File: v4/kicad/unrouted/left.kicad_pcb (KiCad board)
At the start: 2 copper layers, 158 x 119 mm, 68 parts

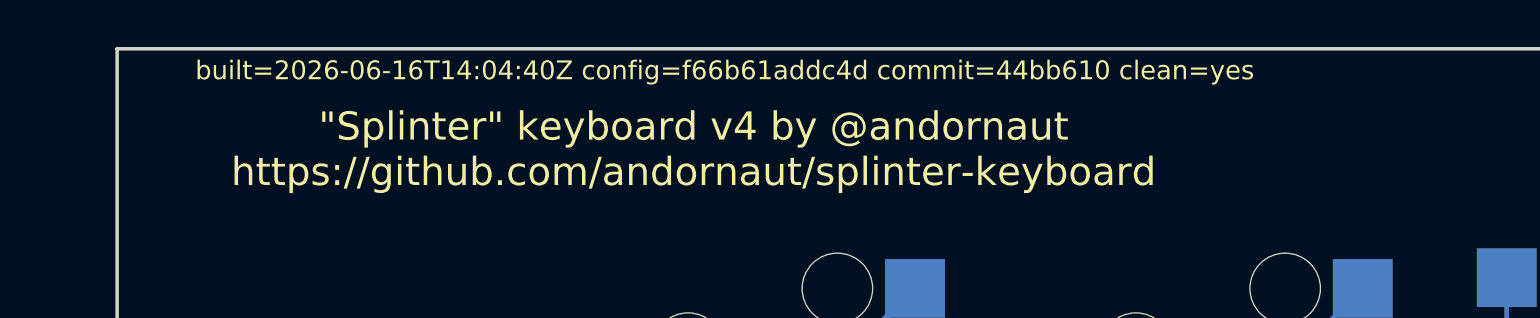
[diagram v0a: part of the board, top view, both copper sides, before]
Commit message: v4: restore right-half teardrops on routed + unrouted masters
The right master carried only 20 teardrop zones (the teardrop-loss
failure that shipped on the first JLCPCB order); re-teardropped to 502,
now symmetric with the left half (464). Tracks, vias, and arcs are
unchanged on both halves (408/70/128 right, 384/65/120 left); the rest
of the diff is KiCad re-save churn. Clears the validate:fab
teardrop-consistency gate.
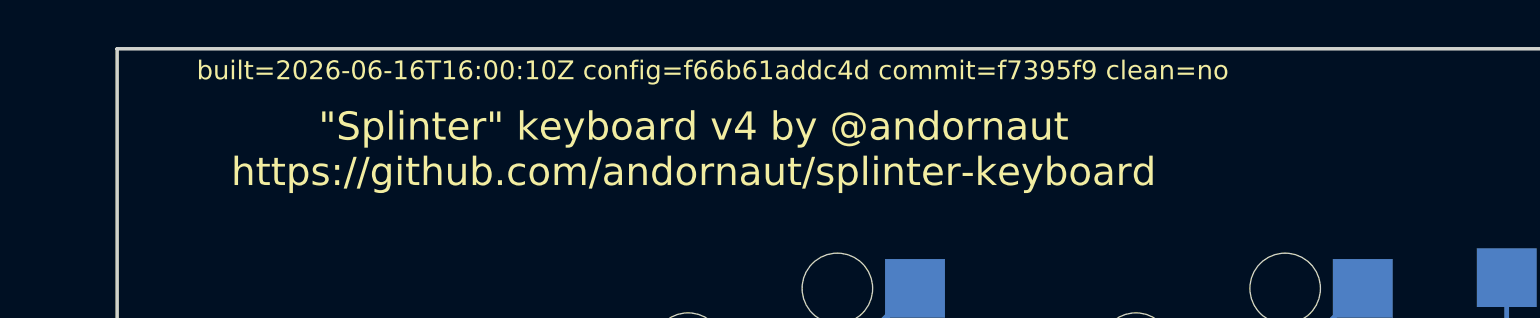
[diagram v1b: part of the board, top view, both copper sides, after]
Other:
- board text added: "built=2026-06-16T16:00:10Z config=f66b61addc4d commit=f7395f9 clean=no"
- board text removed: "built=2026-06-16T14:04:40Z config=f66b61addc4d commit=44bb610 clean=yes"

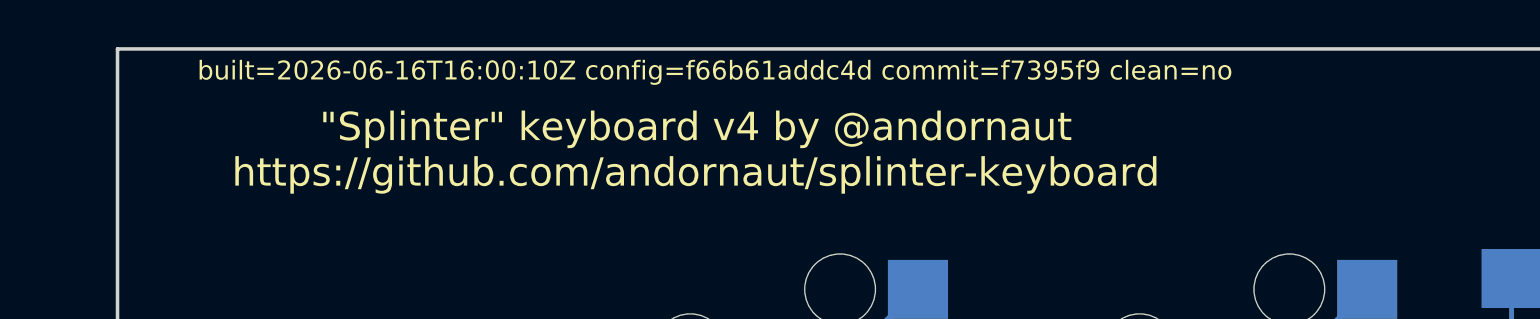
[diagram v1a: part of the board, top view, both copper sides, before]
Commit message: v4: fabrication build (ordering this from JLCPCB)
Validated fab-ready and sent to JLCPCB. Teardrops symmetric (459 left /
496 right zones), GND pour filled on B.Cu (~13000mm^2 master, ~157x118mm
flood in the shipped B_Cu gerber), DRC clean (0 violations / 0 unconnected
both halves), provenance matches config, gerber set + assembly complete.

Provenance stamp (routed masters):
  splinter v=v4 built=2026-06-16T16:30:02Z config=f66b61addc4d commit=d2fd01a clean=yes
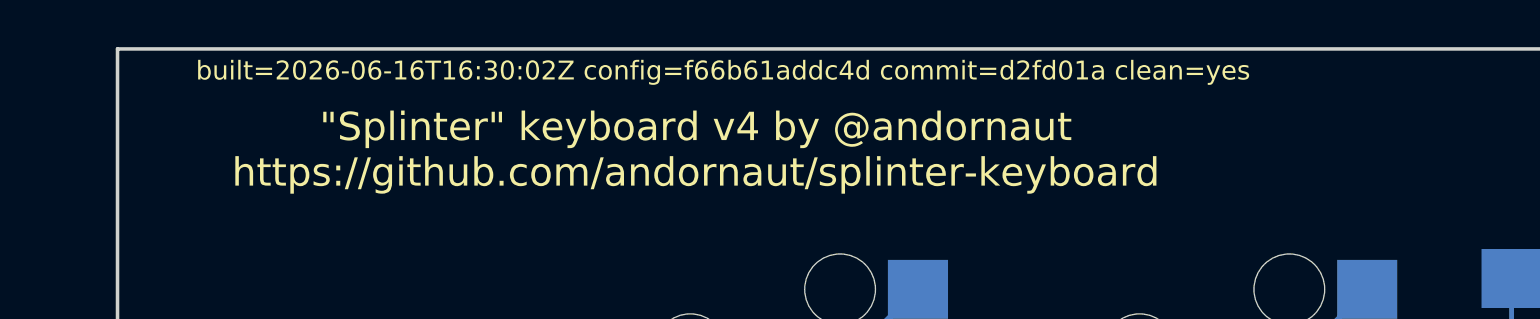
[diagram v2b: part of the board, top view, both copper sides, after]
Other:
- board text added: "built=2026-06-16T16:30:02Z config=f66b61addc4d commit=d2fd01a clean=yes"
- board text removed: "built=2026-06-16T16:00:10Z config=f66b61addc4d commit=f7395f9 clean=no"

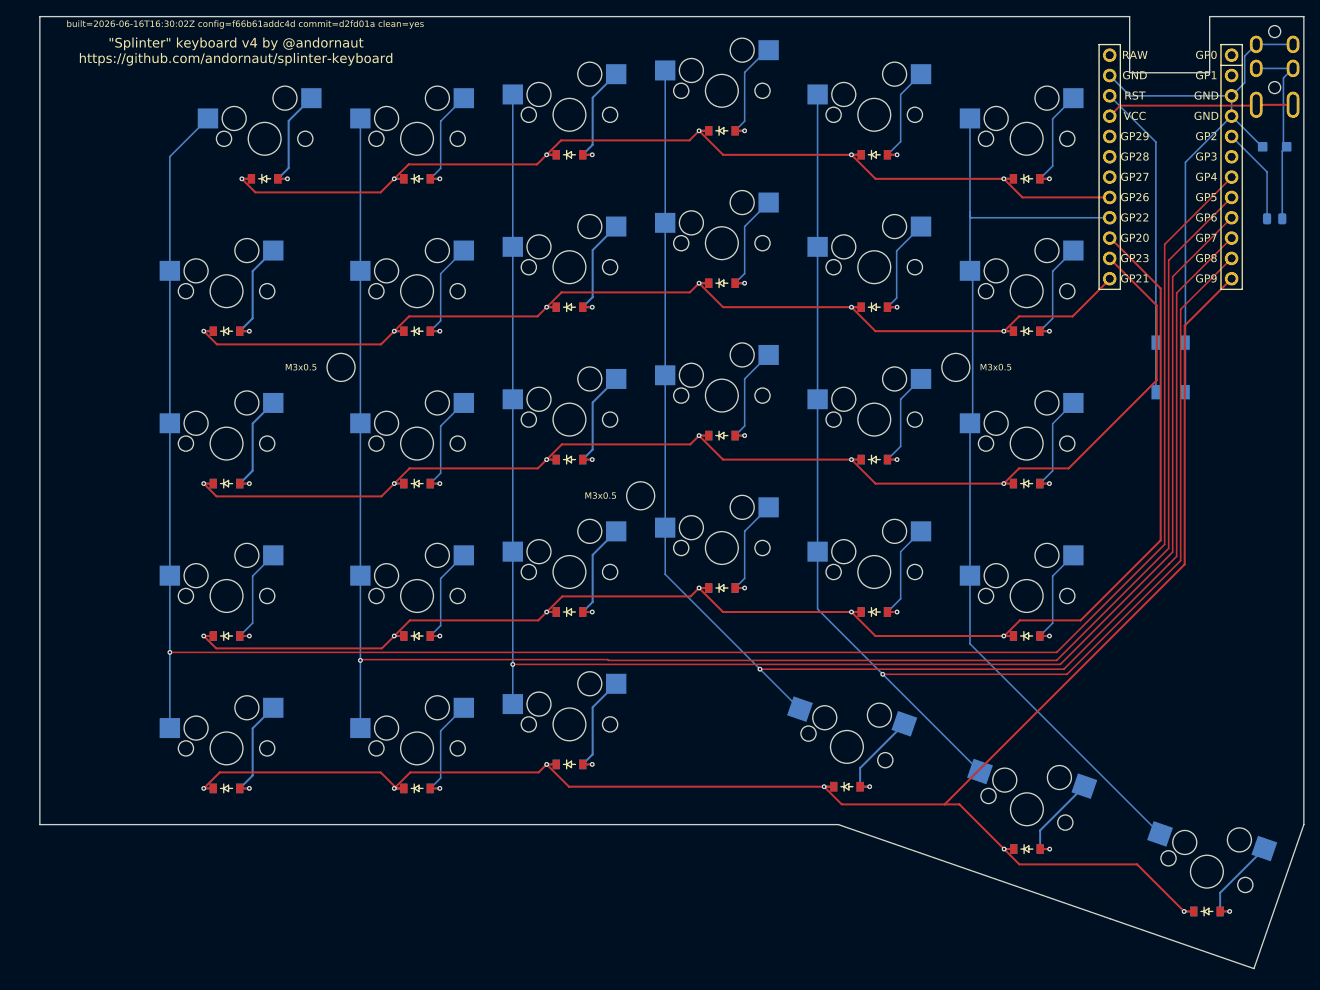
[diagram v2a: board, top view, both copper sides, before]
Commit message: v4: square-cornered USB-C notch, unified 0.25mm clearance, onshape case notes
- config: subtract the USB-C cutout (_usbleft/_usbright) after the exterior
  fillet so the notch keeps square corners; tie it to mcu_reset_x so it tracks
  the MCU. Nudge MCU/reset/TRRS/TVS/resistor placement.
- apply-project-settings: add ensure_default_clearance so the Default net class
  clearance is 0.25mm, unifying the gap with VCC across the board.
- regenerate routed + unrouted boards and project files.
- onshape: add v4 case design guidance (FDM + JLCCNC sandwich topology).
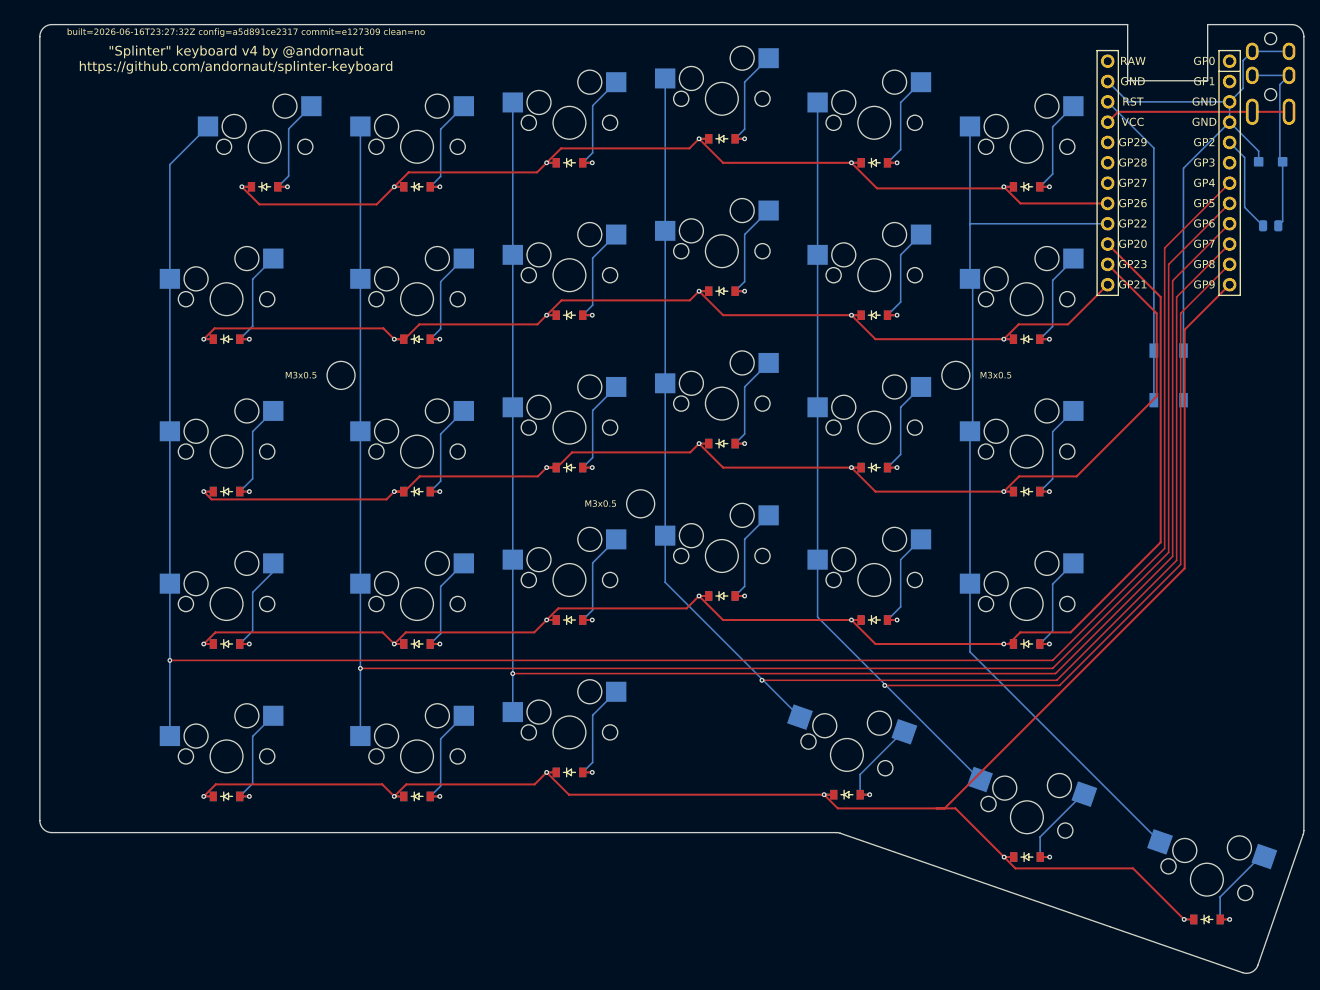
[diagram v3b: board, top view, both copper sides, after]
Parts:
- moved D31 1.94 mm to (284.8, 106.7)
- moved B1 1.03 mm to (272.0, 133.4)
- moved R1 1.01 mm to (284.8, 114.7)
- moved TRRS1 1.01 mm to (284.8, 89.7)
- moved D1 1.00 mm to (154.2, 186.0)
- moved D10 1.00 mm to (178.1, 109.8)
- moved D11 1.00 mm to (197.1, 183.0)
- moved D12 1.00 mm to (197.1, 163.9)
- moved D13 1.00 mm to (197.1, 144.9)
- moved D14 1.00 mm to (197.1, 125.8)
- moved D15 1.00 mm to (197.1, 106.8)
- moved D16 1.00 mm to (216.2, 160.9)
- moved D17 1.00 mm to (216.2, 141.9)
- moved D18 1.00 mm to (216.2, 122.8)
- moved D19 1.00 mm to (216.2, 103.8)
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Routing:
- net P9: track 229.5 -> 228.3 mm
- net GND: track 73.4 -> 74.5 mm
- net zero_lower: track 14.2 -> 13.2 mm
- net P15: track 116.6 -> 115.8 mm
- net P14: track 185.6 -> 184.9 mm
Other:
- board size 158 x 119 mm -> 158 x 118.6 mm
- board text added: "built=2026-06-16T23:27:32Z config=a5d891ce2317 commit=e127309 clean=no"
- board text removed: "built=2026-06-16T16:30:02Z config=f66b61addc4d commit=d2fd01a clean=yes"

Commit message: v4: rebuild boards, restamp provenance clean=yes at fbbf6c4
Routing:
- net P14: track 184.9 -> 186.1 mm
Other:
- board text added: "built=2026-06-17T00:36:15Z config=a5d891ce2317 commit=fbbf6c4 clean=yes"
- board text removed: "built=2026-06-16T23:27:32Z config=a5d891ce2317 commit=e127309 clean=no"

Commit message: checkpoint
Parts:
- removed MH3: , ceoloide:mounting_hole_npth
- moved MH2 42.7 mm to (245.5, 133.4)
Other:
- board text added: "built=2026-06-21T00:07:01Z config=219748922ef7 commit=e35136f clean=no"
- board text removed: "built=2026-06-17T00:36:15Z config=a5d891ce2317 commit=fbbf6c4 clean=yes"

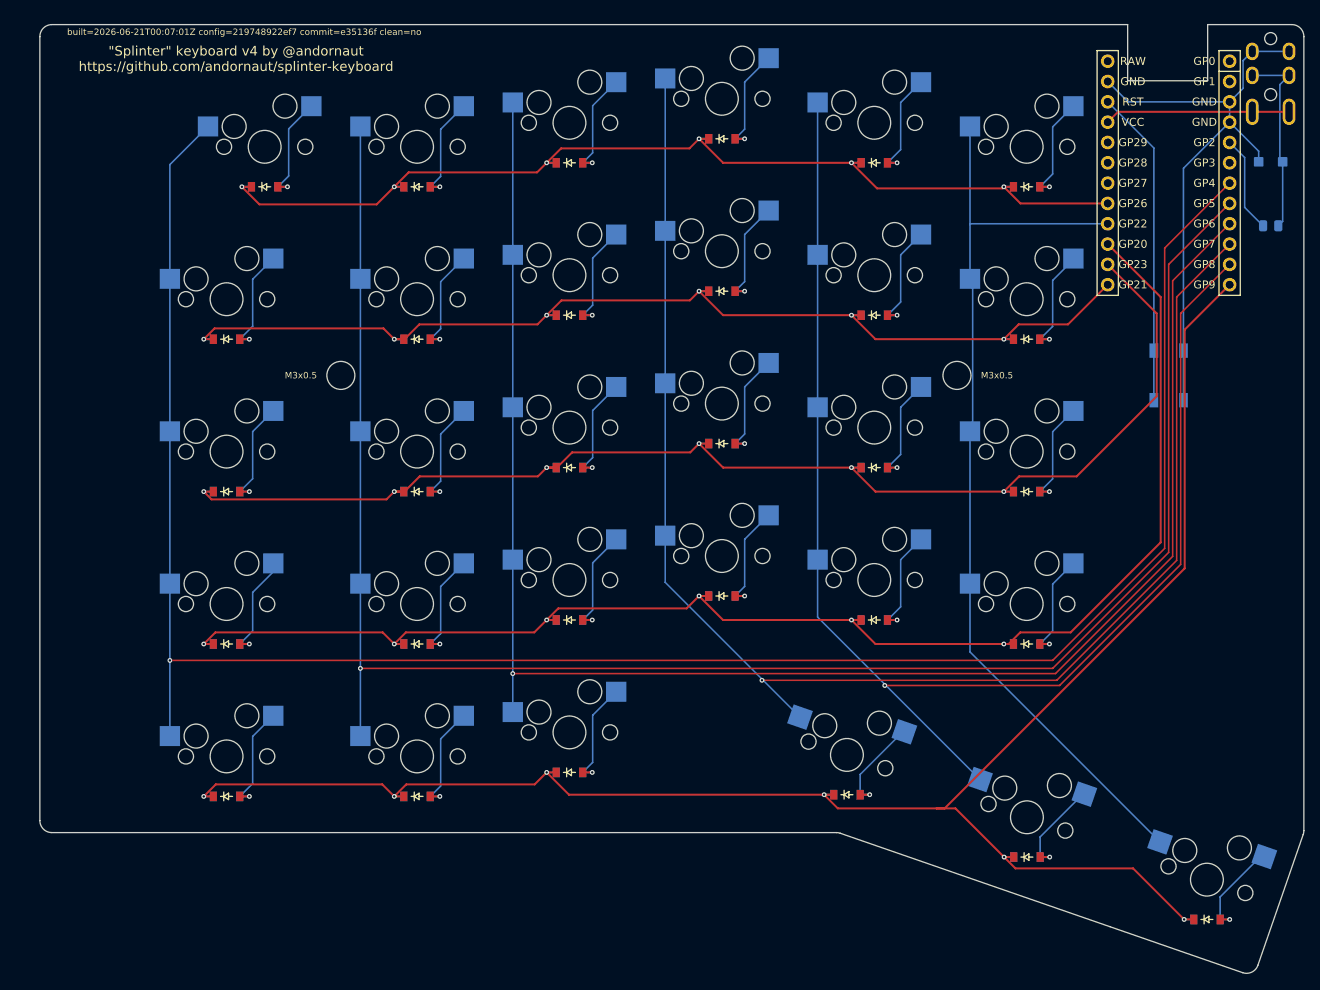
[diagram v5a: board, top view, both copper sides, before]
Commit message: v4: single center support post, retune screws, named boss/support radii
- Replace the three anti-flex support posts with one center-top post
- Reposition screw holes into the diagonal key gaps so the boss clears
  the 14.5mm switch cutouts on both halves
- Promote the boss/support radii to named units (boss 2.5 -> 2.75mm,
  support 2.5 -> 2.25mm) instead of hardcoded literals
- Factor shared silk text geometry into a &text_style YAML anchor
- Trim stale/redundant config comments
- Regenerate unrouted PCBs to match
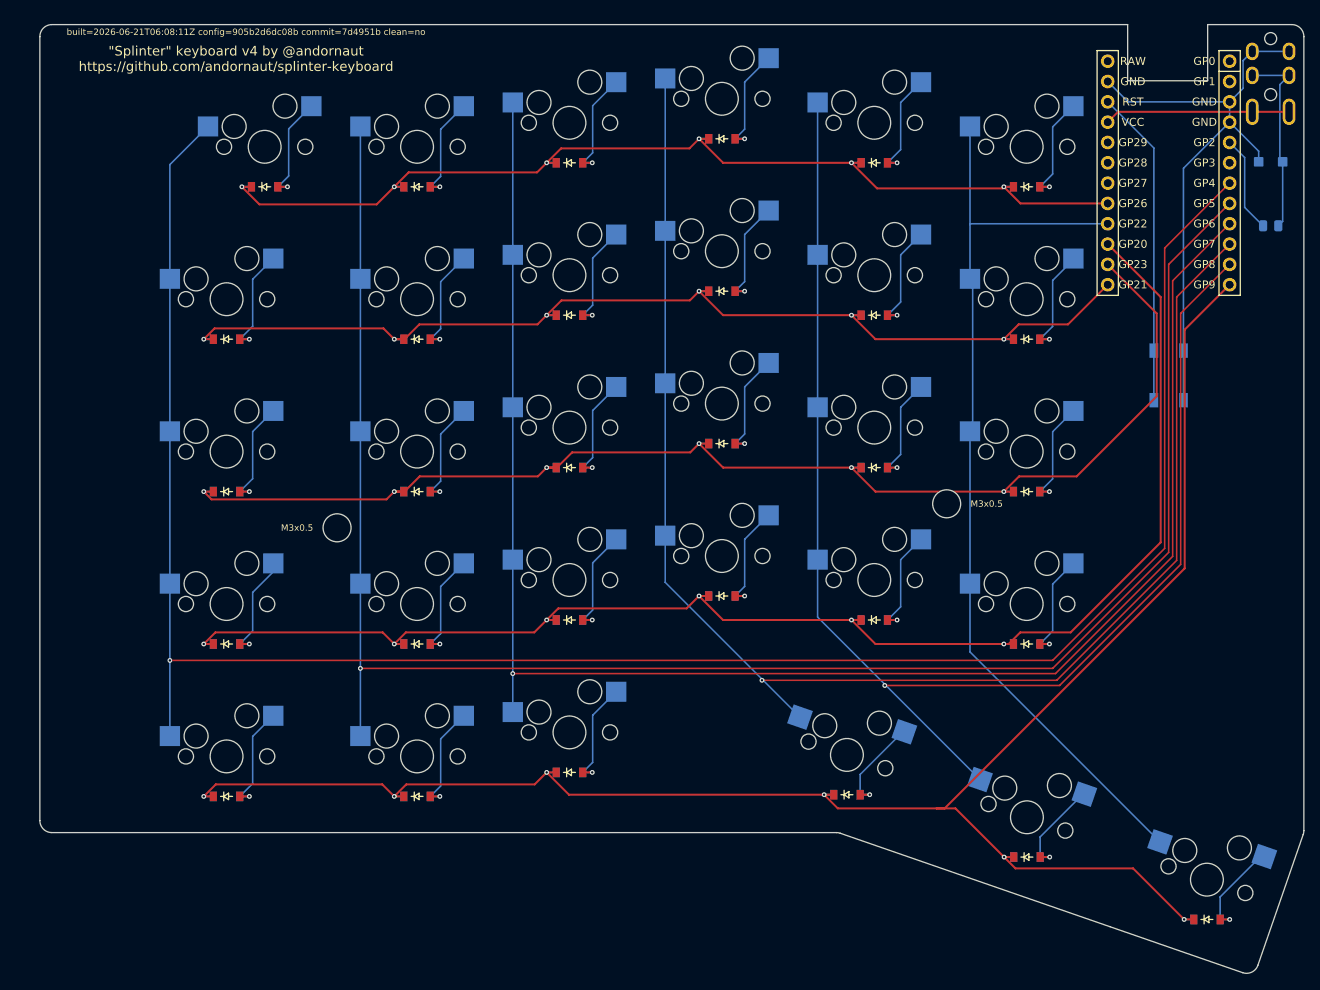
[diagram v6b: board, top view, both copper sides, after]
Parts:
- moved MH1 19.1 mm to (168.1, 152.4)
- moved MH2 16.1 mm to (244.2, 149.4)
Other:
- board text added: "built=2026-06-21T06:08:11Z config=905b2d6dc08b commit=7d4951b clean=no"
- board text removed: "built=2026-06-21T00:07:01Z config=219748922ef7 commit=e35136f clean=no"
